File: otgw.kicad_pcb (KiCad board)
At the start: 2 copper layers, 92 x 60 mm, 44 parts, among them CON1 BARREL_JACK, P2 CONN_01X05, P3 CONN_01X03, P4 CONN_01X02, P5 CONN_01X02, P6 MYSX_2.0, P7 CONN_01X06, Q1 BC558, Q2 BC558, Q3 BC558, Q4 BC547, Q5 BC558, U1 PIC16(L)F88-I/P, U2 PC827, U3 7805

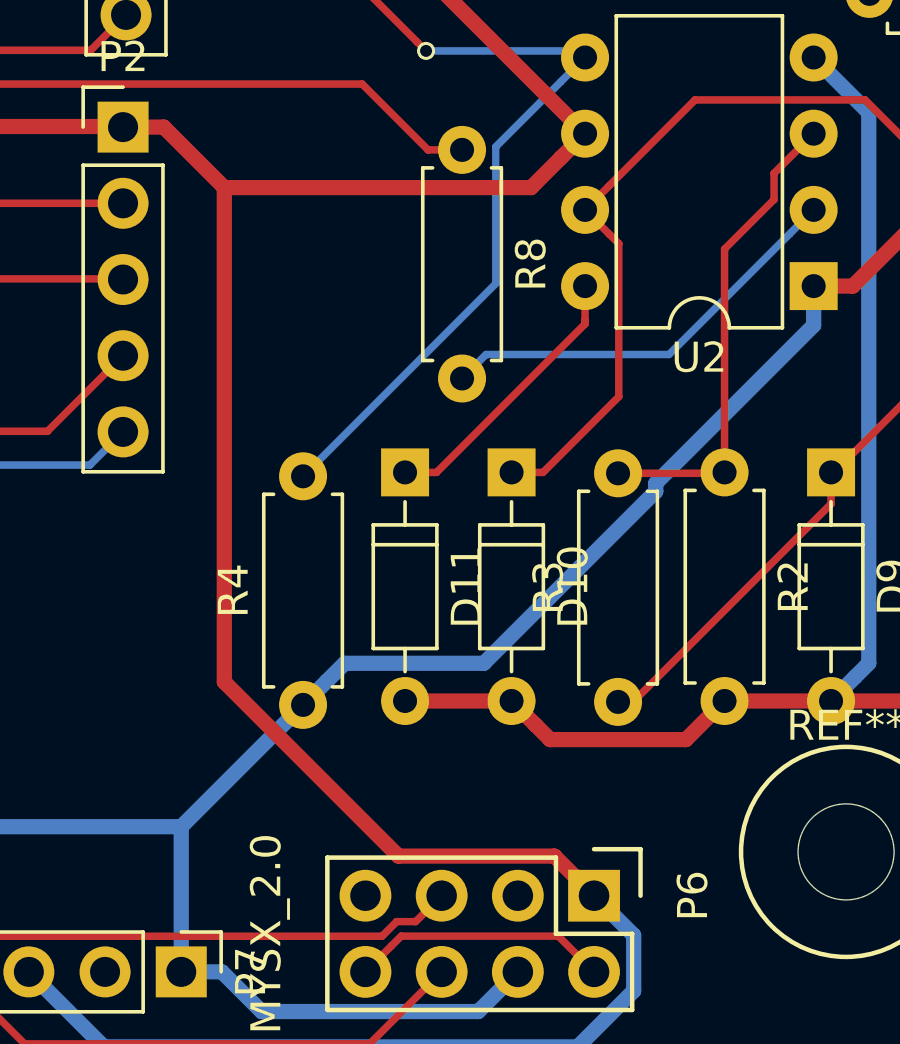
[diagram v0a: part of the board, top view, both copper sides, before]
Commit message: Added a slot for the MYSX cable to go to the other side of the board
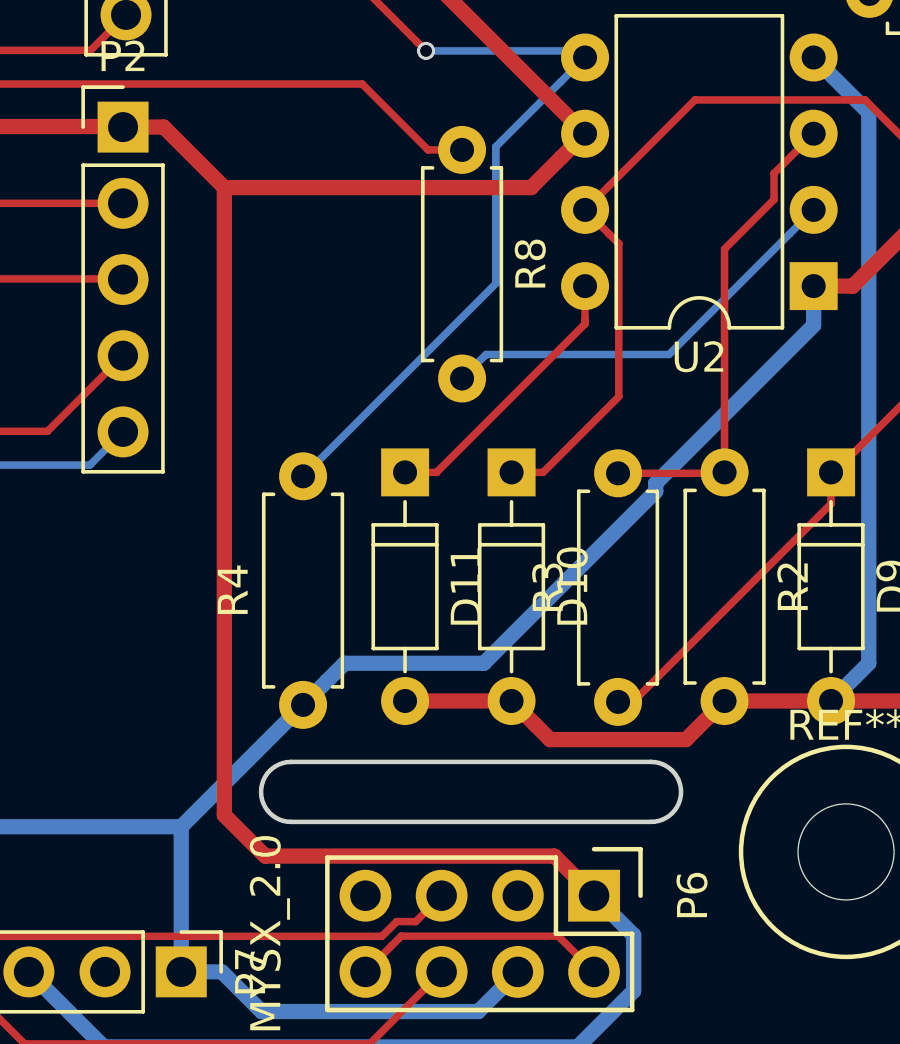
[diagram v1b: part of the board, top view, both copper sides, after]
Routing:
- net VCC: track 161.9 -> 164.5 mm
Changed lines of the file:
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@@
     (links 83)
     (no_connects 0)
-    (area 35.724999 45.724999 137.875 114.275001)
+    (area 35.721799 45.721799 137.8782 114.278201)
     (thickness 1.6)
-    (drawings 0)
+    (drawings 4)
     (tracks 275)
     (zones 0)
@@
     (pad 1 np_thru_hole circle (at 0 0) (size 3.2 3.2) (drill 3.2) (layers *.Cu *.Mask))
   )
+  (gr_line (start 101 101) (end 89 101) (layer Edge.Cuts) (width 0.15))
+  (gr_line (start 89 99) (end 101 99) (layer Edge.Cuts) (width 0.15))
+  (gr_arc (start 101 100) (end 101 99) (angle 180) (layer Edge.Cuts) (width 0.15))
+  (gr_arc (start 89 100) (end 89 101) (angle 180) (layer Edge.Cuts) (width 0.15))
   (segment (start 106.42 83.14) (end 106.42 84.448) (width 0.508) (layer B.Cu) (net 1))
   (segment (start 101.157201 89.710799) (end 101.157201 89.983457) (width 0.508) (layer B.Cu) (net 1))
@@
   (segment (start 62.9 82.9) (end 62.7 82.7) (width 0.25) (layer F.Cu) (net 10))
   (segment (start 99.1 103.46) (end 97.779199 102.139199) (width 0.508) (layer F.Cu) (net 11))
-  (segment (start 97.779199 102.139199) (end 92.578541 102.139199) (width 0.508) (layer F.Cu) (net 11))
-  (segment (start 92.578541 102.139199) (end 86.775201 96.335859) (width 0.508) (layer F.Cu) (net 11))
-  (segment (start 86.775201 96.335859) (end 86.775201 79.857201) (width 0.508) (layer F.Cu) (net 11))
+  (segment (start 97.779199 102.139199) (end 88.139199 102.139199) (width 0.508) (layer F.Cu) (net 11))
+  (segment (start 88.139199 102.139199) (end 86.775201 100.775201) (width 0.508) (layer F.Cu) (net 11))
+  (segment (start 86.775201 100.775201) (end 86.775201 79.857201) (width 0.508) (layer F.Cu) (net 11))
   (segment (start 45.3 67) (end 53.727856 67) (width 0.508) (layer F.Cu) (net 11))
   (segment (start 53.727856 67) (end 54.427856 67.7) (width 0.508) (layer F.Cu) (net 11))
